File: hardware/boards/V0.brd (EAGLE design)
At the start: 45 x 104.5 mm, 140 parts, among them IC2 TPS6300, J1 SJ-43515TS-SMT, J2 HIROSE_DM3BT-DSF-PEJSHIROSE_D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, J3 MOLEX_105450-0101MOLEX_105450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, Q2 ON_SEMI_MMBT5551LT1GON_SEMI_M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, U1 VS1053-L, U2 MICROCHIP_MCP73831T-2ATI-OTMI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, X3 FH12-45S-0.5SH

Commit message: checkpoint: swapped resistors for the esp32/cp2102N/usb port, routed the usb port, and swapped the power source for the CP2102N (runs off the 3.3V regulator now; no sense in the device appearing on computers when it isn't powered on - we'll still be able to charge though)
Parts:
- C22, C23: device rcl:C/6032-28R -> rcl:C0402
- C32, C33: device rcl:C1206 -> rcl:C0402
- R27, R28, R29, R30, R46, R47, R48, R49: device rcl:R0805 -> rcl:R0402
- R31: value 2k -> 1k; device rcl:R0805 -> rcl:R0402
- R50: value 10K -> 10k; device rcl:R0805 -> rcl:R0402
- moved R31 250.0 mm to (7.00, -62.0), flipped to the bottom
- moved D10 86.5 mm to (-1.76, -64.1), flipped to the bottom, turned to 0 degrees
- moved D9 86.1 mm to (2.27, -63.3), flipped to the bottom, turned to 270 degrees
- moved U$3 82.4 mm to (-18.1, 13.1), flipped to the bottom
- moved D8 82.0 mm to (0.26, -63.4), flipped to the bottom, turned to 270 degrees
- moved U$5 67.7 mm to (3.00, 17.0), flipped to the bottom, turned to 180 degrees
- moved U$2 30.0 mm to (44.0, 6.00), turned to 270 degrees
- moved IC2 3.41 mm to (-18.0, 8.59)
- moved C32 1.60 mm to (-6.98, 14.4)
- moved R28 1.06 mm to (-4.01, -64.1), turned to 180 degrees
- moved TP2 1.00 mm to (-8.05, 12.0)
- moved C28 1.00 mm to (-4.00, 9.00)
- moved TPS6224 1.00 mm to (-12.3, 13.7), turned to 0 degrees
- moved R27 0.06 mm to (4.01, -63.9)
- turned JL to 90 degrees
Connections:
- net N$53 renamed CP_RSTB
- removed net CP_VDD: JL.P$6
- net GND: now also C22.2, C23.2; no longer C22.-, C23.-
- net V3P3: now also C22.1, C23.1, JL.P$6, JL.P$7
- net VBAT: no longer C22.+, C23.+, JL.P$7
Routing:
- net V3P3: track 12.2 -> 25.7 mm
- net USB_D-: track 1.94 -> 7.84 mm
- net USB_D+: track 1.61 -> 6.85 mm
- net N$51: track 4.10 -> 8.91 mm, vias 2 -> 0
- net VBAT: track 16.0 -> 19.9 mm
- net N$6: track 0.00 -> 3.67 mm
- net N$8: track 0.00 -> 3.64 mm
- net N$42: track 10.6 -> 9.19 mm
- net V1P8: track 10.1 -> 9.14 mm
- net VBUS: track 8.12 -> 8.66 mm
- net N$3: track 0.00 -> 0.50 mm

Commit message: board checkpoint
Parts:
- J12: value SJ-43515TS-SMT -> 3.5mm TRRS Jack
- moved R29 252.9 mm to (-1.74, -62.5), flipped to the bottom, turned to 180 degrees
- moved R30 247.2 mm to (-4.03, -62.5), flipped to the bottom, turned to 180 degrees
- moved C22 235.0 mm to (-5.30, -59.7), flipped to the bottom
- moved C23 231.4 mm to (-4.00, -59.7), flipped to the bottom
- moved C27 2.00 mm to (-125.0, 92.0)
- moved R4 1.04 mm to (-19.2, -53.0)
- moved R2 1.03 mm to (-17.1, -53.0)
- moved R7 1.03 mm to (-15.1, -53.0)
- moved R6 1.02 mm to (-13.1, -53.0)
- moved R1 1.02 mm to (-11.0, -53.0)
- moved R5 1.02 mm to (-8.99, -53.0)
- moved J2 1.00 mm to (-13.7, -64.2)
- renumbered J1 to J12
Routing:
- net V3P3: track 25.7 -> 33.7 mm, vias 2 -> 4
- net N$52: track 0.00 -> 4.25 mm
- net VBUS: track 8.66 -> 10.3 mm
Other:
- board size 45 x 104.5 mm -> 45 x 104 mm

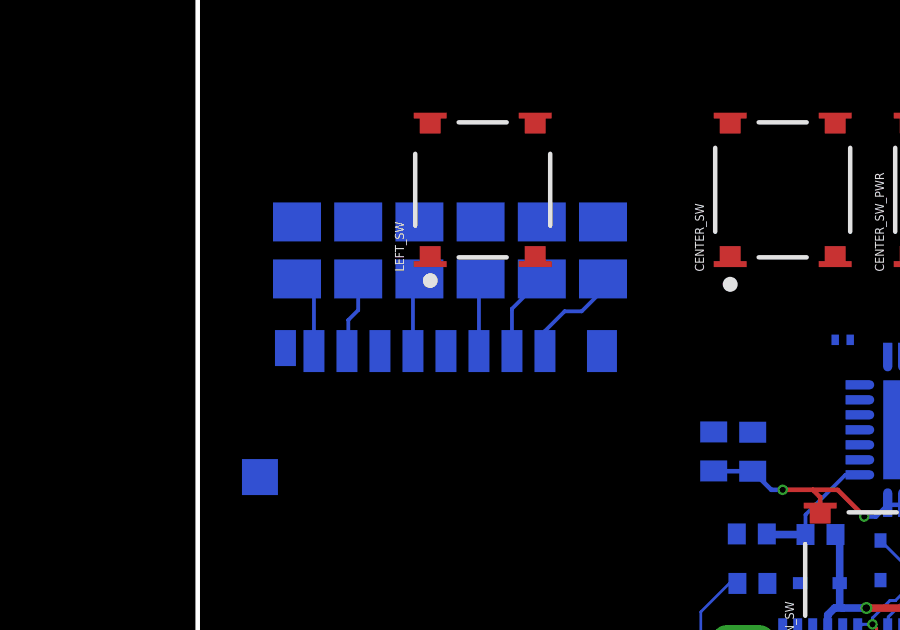
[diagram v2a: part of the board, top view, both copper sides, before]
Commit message: added pull ups to SD card
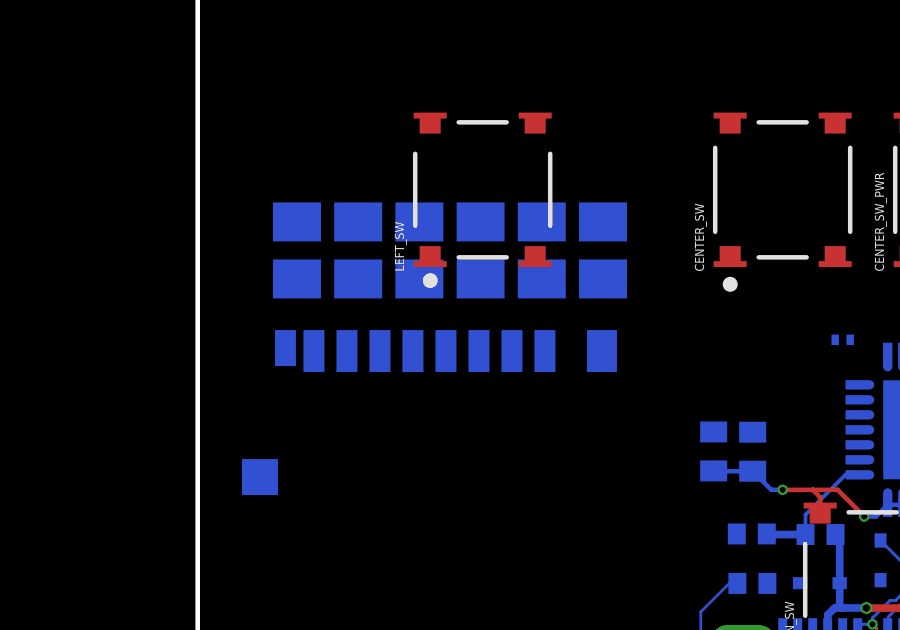
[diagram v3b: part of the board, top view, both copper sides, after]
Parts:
- R1, R2, R4, R5, R6: value 50K -> 10k
- R7: value 10K -> 10k
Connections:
- removed net N$13: J2.2, R1.1
- removed net N$15: J2.8, R4.1
- removed net N$17: J2.1, R5.1
- removed net N$2: J2.7, R2.1
- removed net N$7: J2.3, R6.1
- removed net N$9: J2.5, R7.1
- net IO12: now also J2.1, R4.1; no longer R5.2
- net IO13: now also J2.2, R5.1; no longer R1.2
- net IO14: now also J2.5, R6.1; no longer R7.2
- net IO15: now also J2.3, R7.1; no longer R6.2
- net IO2: now also J2.7, R1.1; no longer R2.2
- net IO4: now also J2.8, R2.1; no longer R4.2
- net V3P3: now also R1.2, R2.2, R4.2, R5.2, R6.2, R7.2
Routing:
- net N$17: track 3.54 -> 0.00 mm
- net N$13: track 2.82 -> 0.00 mm
- net N$15: track 2.64 -> 0.00 mm
- net N$2: track 2.56 -> 0.00 mm
- net N$9: track 2.49 -> 0.00 mm
- net N$7: track 2.43 -> 0.00 mm

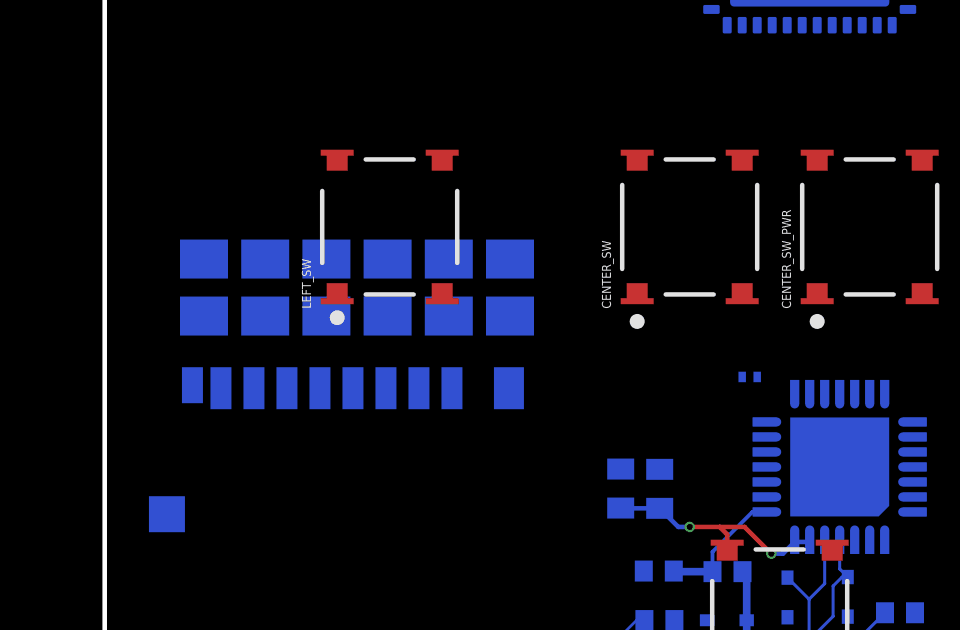
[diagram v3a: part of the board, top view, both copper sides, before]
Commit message: Swap resistors for the microSD Card
10k pull-ups on everything appears to work (50k does not even though some of the guides say otherwise).

Only 1-line MMC mode works so far, but there's still stuff to try.
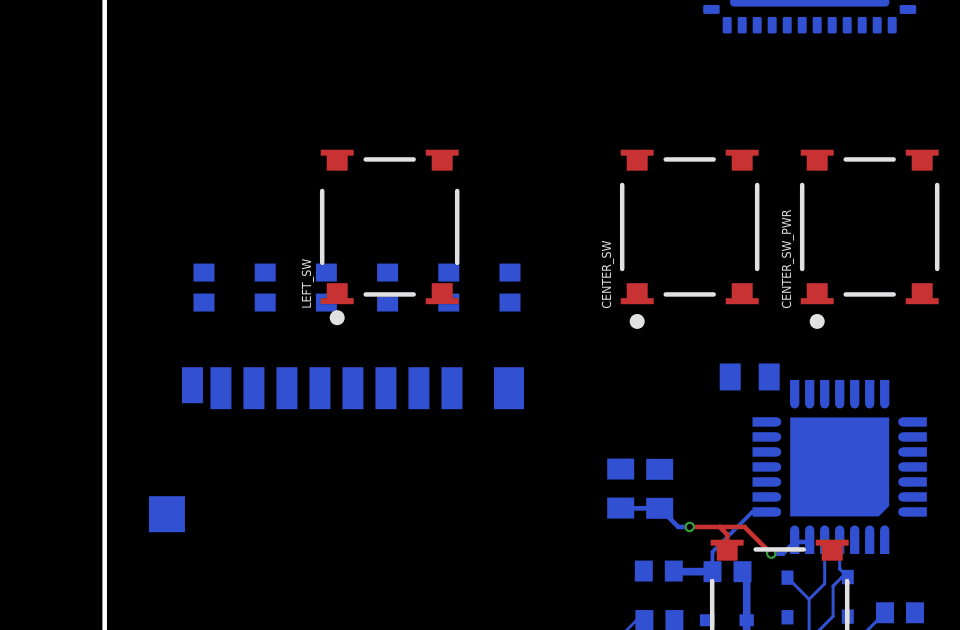
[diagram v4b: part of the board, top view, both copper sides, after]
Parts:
- C1: device rcl:C0201 -> rcl:C0402
- R1, R2, R4, R5, R6, R7: device adafruit:M0805 -> rcl:R0402

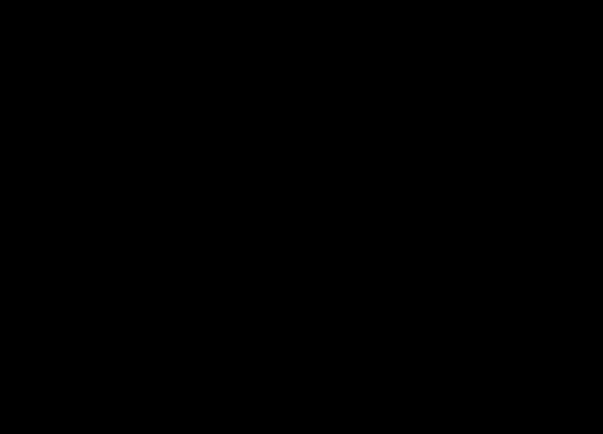
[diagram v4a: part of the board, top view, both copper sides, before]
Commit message: Add an experimental card detect input to the ADC button circuit
If this is problematic we can just remove/not populate the resistor for CARD_DETECT (R54). Just adding an input to the ADC and not the full diode + digital input line too because we can just poll the ADC when we have SD card errors to make sure we've got a card in place (I'd rather not add another one of those diodes).
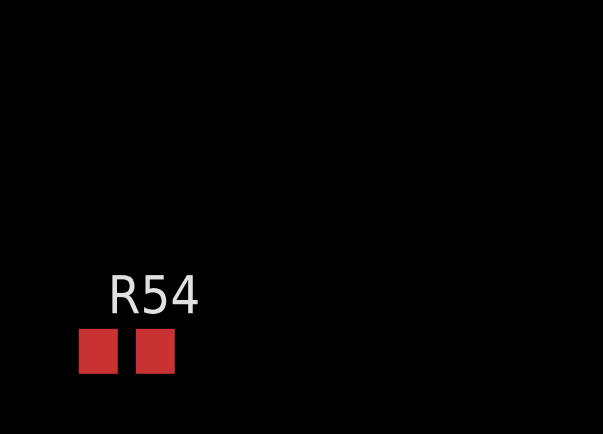
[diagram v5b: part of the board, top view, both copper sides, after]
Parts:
- added R54: 315k, rcl:R0805
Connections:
- new net CARD_DETECT: J2.9, R54.2
- net BUTTON_ADC: now also R54.1
- net V3P3: now also J2.10
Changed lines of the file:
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@@
 <attribute name="VALUE" x="140.54" y="85.365" size="1.27" layer="27" rot="R90"/>
+</element>
+<element name="R54" library="rcl" library_urn="urn:adsk.eagle:library:334" package="R0805" package3d_urn="urn:adsk.eagle:package:23553/2" value="315k" x="-170.5" y="-173" smashed="yes">
+<attribute name="NAME" x="-171.135" y="-171.73" size="1.27" layer="25"/>
+<attribute name="SPICEPREFIX" value="R" x="-170.5" y="-173" size="1.778" layer="27" display="off"/>
+<attribute name="VALUE" x="-171.135" y="-175.54" size="1.27" layer="27"/>
 </element>
 </elements>
@@
 <contactref element="R7" pad="2"/>
 <contactref element="R6" pad="2"/>
+<contactref element="J2" pad="10"/>
 <wire x1="-36.4" y1="-45.425" x2="-60" y2="-41" width="0" layer="19" extent="1-1"/>
 <wire x1="-19.19" y1="-52.52" x2="-36.4" y2="-45.425" width="0" layer="19" extent="1-16"/>
@@
 <wire x1="-1.75" y1="-61.525" x2="-1.75" y2="-61.25" width="0" layer="19" extent="1-1"/>
 <wire x1="7" y1="-61.5" x2="1" y2="-61.5" width="0" layer="19" extent="16-16"/>
+<wire x1="-20.425" y1="-66.775" x2="-14.225" y2="-56.375" width="0" layer="19" extent="16-16"/>
 <wire x1="-16.975" y1="-28.0822" x2="-1.75" y2="-35.525" width="0" layer="19" extent="1-16"/>
 <wire x1="-18.925" y1="-28.0822" x2="-16.975" y2="-28.0822" width="0" layer="19" extent="16-16"/>
@@
 <contactref element="R25" pad="2"/>
 <contactref element="U$1" pad="10"/>
+<contactref element="R54" pad="1"/>
 <wire x1="-60.05" y1="-72" x2="-60.05" y2="-77" width="0" layer="19" extent="1-1"/>
 <wire x1="-60.05" y1="-67" x2="-60.05" y2="-72" width="0" layer="19" extent="1-1"/>
@@
 <wire x1="-61.95" y1="-35" x2="-60.05" y2="-57" width="0" layer="19" extent="1-1"/>
 <wire x1="4.275" y1="-42.75" x2="-60.05" y2="-57" width="0" layer="19" extent="1-16"/>
+<wire x1="-171.45" y1="-173" x2="-60.05" y2="-77" width="0" layer="19" extent="1-1"/>
 </signal>
 <signal name="BUTTON_DIN">
@@
 <wire x1="-1.25" y1="-48.525" x2="-1.25" y2="-48.875" width="0" layer="19" extent="1-1"/>
 </signal>
+<signal name="CARD_DETECT">
+<contactref element="R54" pad="2"/>
+<contactref element="J2" pad="9"/>
+<wire x1="-19.575" y1="-56.275" x2="-169.55" y2="-173" width="0" layer="19" extent="1-16"/>
+</signal>
 </signals>

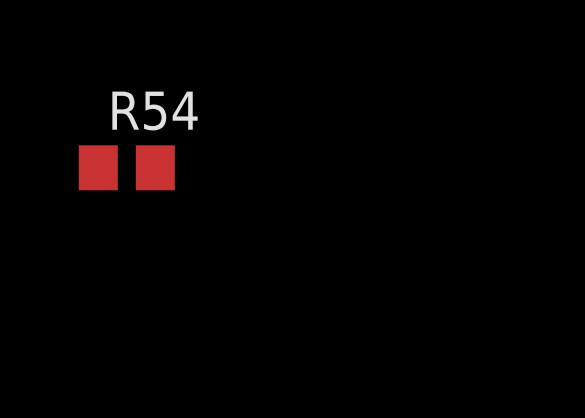
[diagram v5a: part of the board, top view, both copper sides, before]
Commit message: Bridge IO0 and IO2 so that we can flash the board and use an SD Card
From the message on sheet 1:
IO2 is a strapping pin that allows the esp32 to enter download mode (iirc) - it's required to be pulled low when flashing the esp. Unforuntately, we have to use IO2 for the one usable SD/MMC interface on the esp32 (the other uses the same pins as flash).

IO0 is also a strapping pin: it's connected to RTS on the CP2102N and is pulled low when we're flashing the board. So, if we tie IO0 to IO2, IO2 will be pulled down while flashing. This solves our problem!

Unforunately this means that we can't use IO0 for anything else since it remains tied to IO2 (anything we do to IO0 will affect the SD/MMC peripheral). We could use a fancy circuit that pulls IO2 low only when the chip is reset (for a second or so) or do some transistor magic (only pull IO2 low when multiple other pins are low or something), but since we're only using IO0 for an LED, I figure it's not worth the trouble.

We'll move the LED's net to something else and connect IO0 and IO2.

Ended up putting the green and blue LEDs on the same pin. Since the voltage drops are different, hopefully we can get slightly different colors by PWMing at different frequencies.
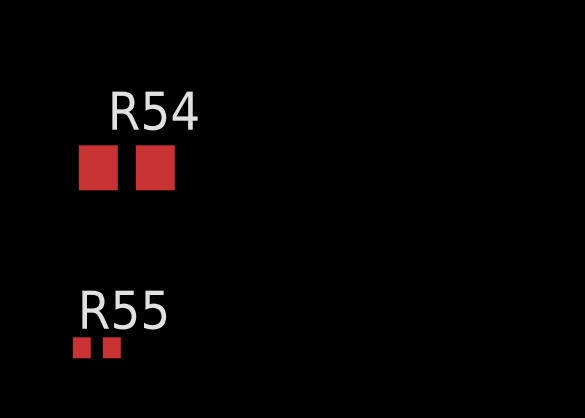
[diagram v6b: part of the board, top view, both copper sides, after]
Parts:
- added R55: 25, rcl:R0402
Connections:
- removed net GREEN_LED_CATH: R36.2, U$1.28
- new net BLUE_GREEN_LED_CATH: R36.2, R55.2, U$1.28
- new net N$2: D1.1, R55.1
- net IO0: no longer D1.1, U$1.23
- net IO2: now also U$1.23
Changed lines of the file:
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@@
 <attribute name="VALUE" x="-171.135" y="-175.54" size="1.27" layer="27"/>
+</element>
+<element name="R55" library="rcl" library_urn="urn:adsk.eagle:library:334" package="R0402" package3d_urn="urn:adsk.eagle:package:23547/3" value="25" x="-171.5" y="-179" smashed="yes">
+<attribute name="NAME" x="-172.135" y="-178.365" size="1.27" layer="25"/>
+<attribute name="SPICEPREFIX" value="R" x="-171.5" y="-179" size="1.778" layer="27" display="off"/>
+<attribute name="VALUE" x="-172.135" y="-180.905" size="1.27" layer="27"/>
 </element>
 </elements>
@@
 <contactref element="J2" pad="7"/>
 <contactref element="R1" pad="1"/>
+<contactref element="U$1" pad="23"/>
 <wire x1="-11.03" y1="-53.52" x2="-17.525" y2="-56.375" width="0" layer="19" extent="16-16"/>
-<wire x1="-0.75" y1="-44.275" x2="-11.03" y2="-53.52" width="0" layer="19" extent="16-16"/>
+<wire x1="-1.25" y1="-44.275" x2="-11.03" y2="-53.52" width="0" layer="19" extent="16-16"/>
+<wire x1="-0.75" y1="-44.275" x2="-1.25" y2="-44.275" width="0" layer="19" extent="16-16"/>
 </signal>
 <signal name="IO14">
@@
 <wire x1="-109" y1="91.05" x2="-36.75" y2="-43.675" width="0" layer="19" extent="1-1"/>
 </signal>
-<signal name="GREEN_LED_CATH">
-<contactref element="R36" pad="2"/>
-<contactref element="U$1" pad="28"/>
-<wire x1="-109" y1="92.95" x2="-2.275" y2="-42.25" width="0" layer="19" extent="1-16"/>
-</signal>
 <signal name="SYS_ENABLE">
 <contactref element="IC2" pad="6"/>
@@
 <signal name="IO0">
 <contactref element="Q3" pad="3"/>
-<contactref element="U$1" pad="23"/>
-<contactref element="D1" pad="1"/>
-<wire x1="-1.25" y1="-44.275" x2="61.9" y2="87" width="0" layer="19" extent="1-16"/>
-<wire x1="-36.75" y1="-46.325" x2="-1.25" y2="-44.275" width="0" layer="19" extent="1-16"/>
 </signal>
 <signal name="IO15">
@@
 <wire x1="-19.575" y1="-56.275" x2="-169.55" y2="-173" width="0" layer="19" extent="1-16"/>
 </signal>
+<signal name="N$2">
+<contactref element="D1" pad="1"/>
+<contactref element="R55" pad="1"/>
+<wire x1="-36.75" y1="-46.325" x2="-172" y2="-179" width="0" layer="19" extent="1-1"/>
+</signal>
+<signal name="BLUE_GREEN_LED_CATH">
+<contactref element="R55" pad="2"/>
+<contactref element="R36" pad="2"/>
+<contactref element="U$1" pad="28"/>
+<wire x1="-2.275" y1="-42.25" x2="-171" y2="-179" width="0" layer="19" extent="1-16"/>
+<wire x1="-109" y1="92.95" x2="-2.275" y2="-42.25" width="0" layer="19" extent="1-16"/>
+</signal>
 </signals>

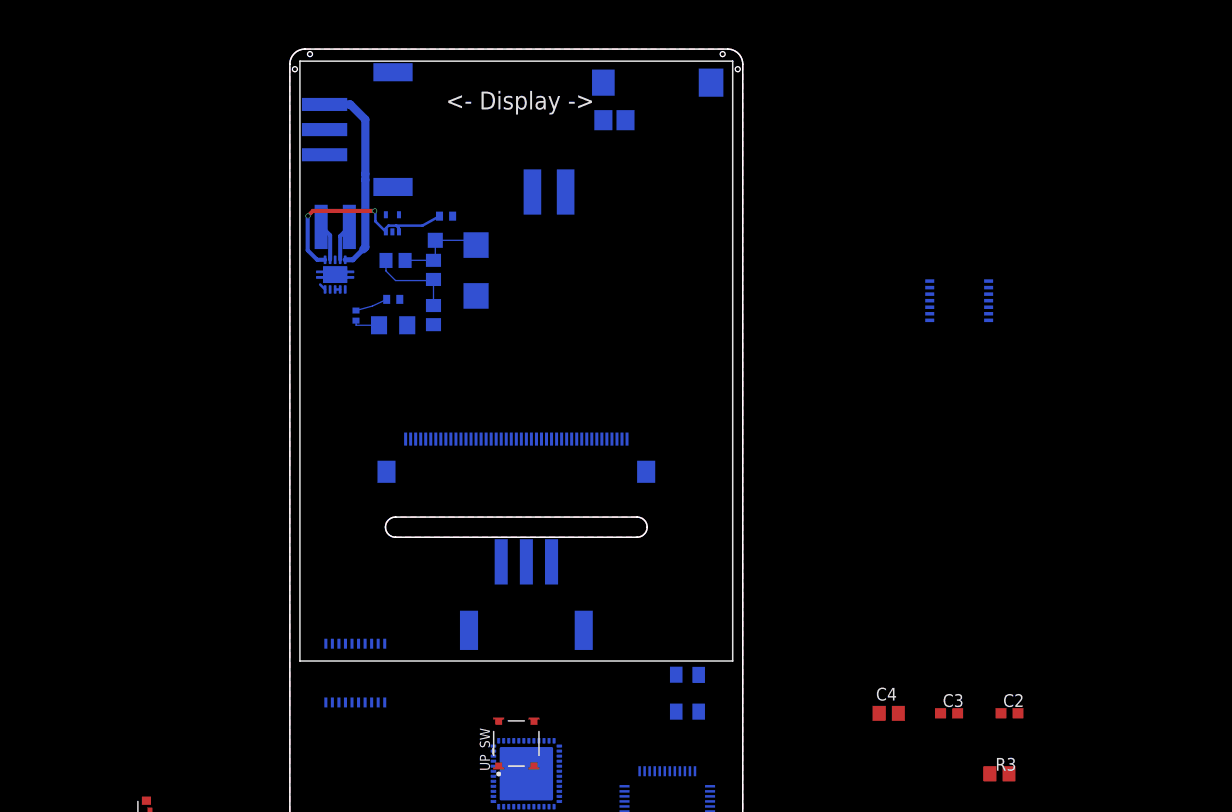
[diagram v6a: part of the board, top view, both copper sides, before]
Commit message: magnet positions: a guess
the BOM is updated now too; gonna go with [these magnets](https://www.ebay.com/itm/1-100-Rare-Earth-Magnets-Neodymium-Round-Disk-Super-Strong-Large-Sizes-USA/122945482155), probably

this closes #14
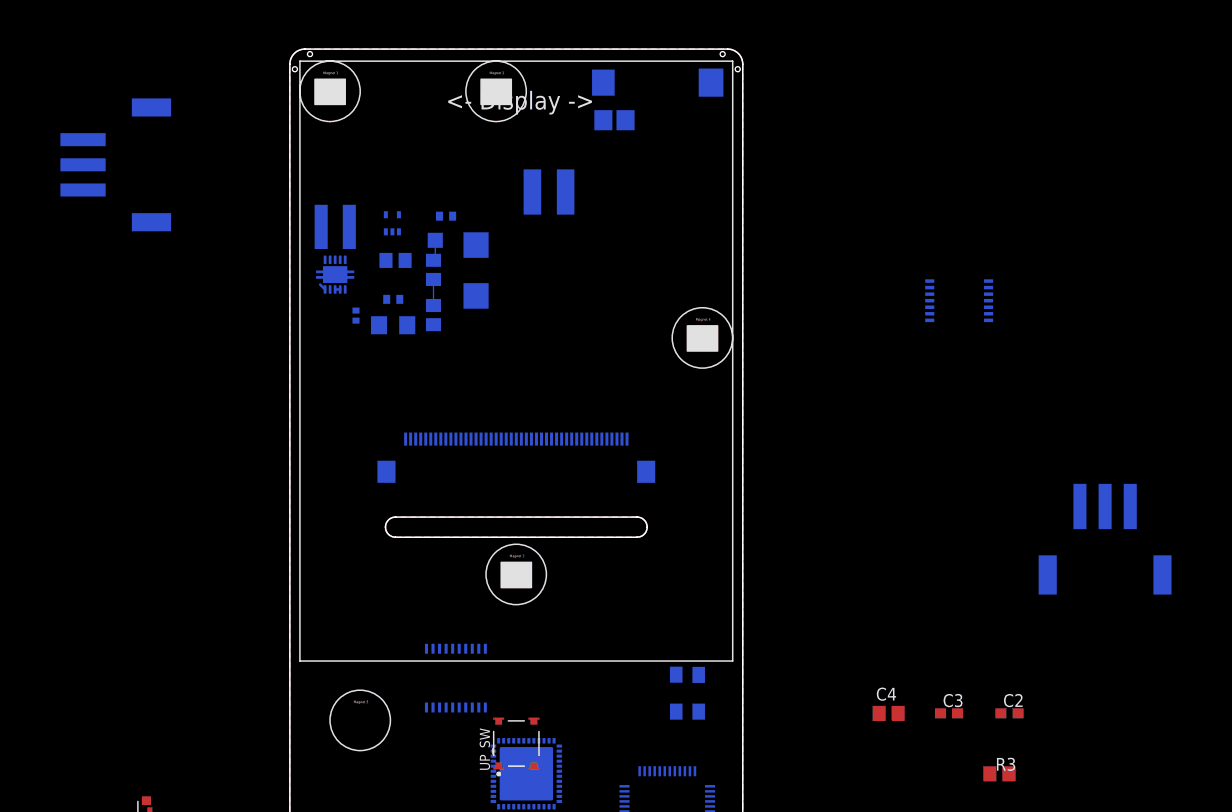
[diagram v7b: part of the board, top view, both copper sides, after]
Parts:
- moved VIBM_CON 57.8 mm to (58.5, -19.5)
- moved BATT_CON 24.3 mm to (-38.0, 19.5)
- moved U$6 10.0 mm to (-6.00, -31.5)
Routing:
- net V3P3: track 33.7 -> 8.76 mm, vias 4 -> 2
- net VBAT: track 19.9 -> 0.00 mm
- net V1P8: track 9.14 -> 1.82 mm
- net N$42: track 9.19 -> 3.14 mm
- net N$8: track 3.64 -> 0.00 mm
- net N$6: track 3.67 -> 0.06 mm
- net EN: track 2.74 -> 0.00 mm
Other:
- board text added: "Magnet 1"
- board text added: "Magnet 2"
- board text added: "Magnet 3"
- board text added: "Magnet 4"
- board text added: "Magnet 5"
